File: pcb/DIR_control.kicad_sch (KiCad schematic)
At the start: 31 parts, among them J3 Conn_01x04_Socket, Q2 AO3416A, SW2 SW_DIP_x02, SW3 SW_SPST, SW4 SW_SPST, SW5 SW_SPST, U3 AT24CM02-SSHM, U4 ATtiny1604-SS, U5 FT230XS

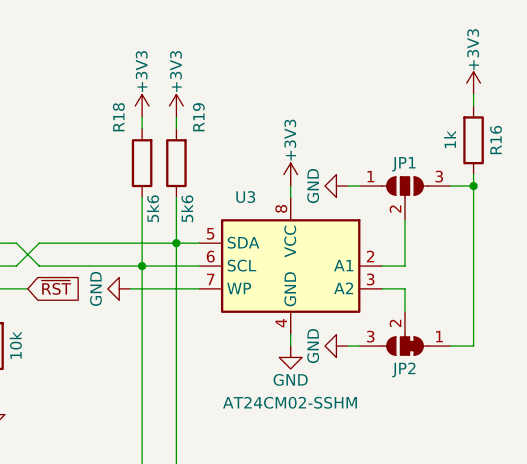
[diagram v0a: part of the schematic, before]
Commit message: Change Z-Diode to 3V3
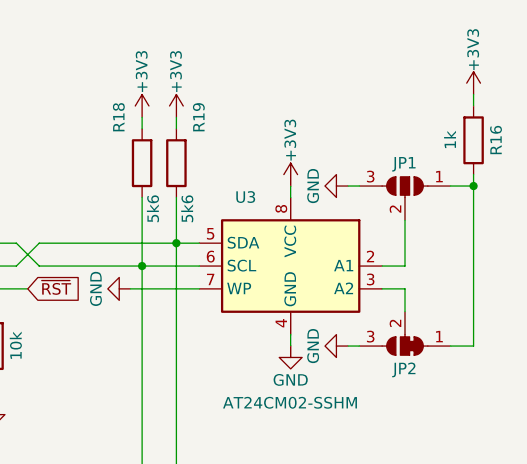
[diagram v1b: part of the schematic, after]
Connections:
- net GND: now also JP1.3 (B); no longer JP1.1 (A)
- net at JP2.1 (A), R16.1: now also JP1.1 (A); no longer JP1.3 (B)
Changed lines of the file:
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@@
     )
   )
-  (symbol (lib_id "Jumper:SolderJumper_3_Open") (at 241.3 64.77 0) (unit 1)
+  (symbol (lib_id "Jumper:SolderJumper_3_Open") (at 241.3 64.77 0) (mirror y) (unit 1)
     (in_bom yes) (on_board yes) (dnp no)
     (property "Reference" "JP1" (at 241.3 62.23 0)
